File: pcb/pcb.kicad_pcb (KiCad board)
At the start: 2 copper layers, 8 parts, among them J1 Conn_01x04_Pin, J2 Conn_01x06_Pin, U1 XIAO-ESP32-C5-DIP, U17 AP2112K-3.3

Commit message: tidy up warnings
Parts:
- added R10: 10k, Resistor_THT:R_Axial_DIN0204_L3.6mm_D1.6mm_P5.08mm_Horizontal, F.Cu at (154.4, 117.5)
- added R11: 10k, Resistor_THT:R_Axial_DIN0204_L3.6mm_D1.6mm_P5.08mm_Horizontal, F.Cu at (154.4, 120.6)
- added R12: 10k, Resistor_THT:R_Axial_DIN0204_L3.6mm_D1.6mm_P5.08mm_Horizontal, F.Cu at (154.4, 123.8)
- added R13: 10k, Resistor_THT:R_Axial_DIN0204_L3.6mm_D1.6mm_P5.08mm_Horizontal, F.Cu at (162.4, 108.0)
- added R14: 10k, Resistor_THT:R_Axial_DIN0204_L3.6mm_D1.6mm_P5.08mm_Horizontal, F.Cu at (162.4, 111.2)
- added R15: 10k, Resistor_THT:R_Axial_DIN0204_L3.6mm_D1.6mm_P5.08mm_Horizontal, F.Cu at (162.4, 114.3)
- added R16: 10k, Resistor_THT:R_Axial_DIN0204_L3.6mm_D1.6mm_P5.08mm_Horizontal, F.Cu at (162.4, 117.5)
- added R17: 10k, Resistor_THT:R_Axial_DIN0204_L3.6mm_D1.6mm_P5.08mm_Horizontal, F.Cu at (162.4, 120.6)
- added R3: 10k, Resistor_THT:R_Axial_DIN0204_L3.6mm_D1.6mm_P5.08mm_Horizontal, F.Cu at (146.3, 114.3)
- added R4: 10k, Resistor_THT:R_Axial_DIN0204_L3.6mm_D1.6mm_P5.08mm_Horizontal, F.Cu at (146.3, 117.5)
- added R5: 10k, Resistor_THT:R_Axial_DIN0204_L3.6mm_D1.6mm_P5.08mm_Horizontal, F.Cu at (146.3, 120.6)
- added R6: 10k, Resistor_THT:R_Axial_DIN0204_L3.6mm_D1.6mm_P5.08mm_Horizontal, F.Cu at (146.3, 123.8)
- added R7: 10k, Resistor_THT:R_Axial_DIN0204_L3.6mm_D1.6mm_P5.08mm_Horizontal, F.Cu at (154.4, 108.0)
- added R8: 10k, Resistor_THT:R_Axial_DIN0204_L3.6mm_D1.6mm_P5.08mm_Horizontal, F.Cu at (154.4, 111.2)
- added R9: 10k, Resistor_THT:R_Axial_DIN0204_L3.6mm_D1.6mm_P5.08mm_Horizontal, F.Cu at (154.4, 114.3)
- added U10: XIAO-ESP32-C5-DIP, xiao_footprints:XIAO-ESP32-C5-DIP, F.Cu at (108.7, 66.0)
- added U11: XIAO-ESP32-C5-DIP, xiao_footprints:XIAO-ESP32-C5-DIP, F.Cu at (108.7, 86.4)
- added U12: XIAO-ESP32-C5-DIP, xiao_footprints:XIAO-ESP32-C5-DIP, F.Cu at (108.7, 106.7)
- added U13: XIAO-ESP32-C5-DIP, xiao_footprints:XIAO-ESP32-C5-DIP, F.Cu at (132.3, 45.7)
- added U14: XIAO-ESP32-C5-DIP, xiao_footprints:XIAO-ESP32-C5-DIP, F.Cu at (132.3, 66.0)
- added U15: XIAO-ESP32-C5-DIP, xiao_footprints:XIAO-ESP32-C5-DIP, F.Cu at (132.3, 86.4)
- added U18: XIAO-ESP32-C5-DIP, xiao_footprints:XIAO-ESP32-C5-DIP, F.Cu at (132.3, 106.7)
- added U2: XIAO-ESP32-C5-DIP, xiao_footprints:XIAO-ESP32-C5-DIP, F.Cu at (61.5, 66.0)
- added U3: XIAO-ESP32-C5-DIP, xiao_footprints:XIAO-ESP32-C5-DIP, F.Cu at (61.5, 86.4)
- added U4: XIAO-ESP32-C5-DIP, xiao_footprints:XIAO-ESP32-C5-DIP, F.Cu at (61.5, 106.7)
- added U5: XIAO-ESP32-C5-DIP, xiao_footprints:XIAO-ESP32-C5-DIP, F.Cu at (85.1, 45.7)
- added U6: XIAO-ESP32-C5-DIP, xiao_footprints:XIAO-ESP32-C5-DIP, F.Cu at (85.1, 66.0)
- added U7: XIAO-ESP32-C5-DIP, xiao_footprints:XIAO-ESP32-C5-DIP, F.Cu at (85.1, 86.4)
- added U8: XIAO-ESP32-C5-DIP, xiao_footprints:XIAO-ESP32-C5-DIP, F.Cu at (85.1, 106.7)
- added U9: XIAO-ESP32-C5-DIP, xiao_footprints:XIAO-ESP32-C5-DIP, F.Cu at (108.7, 45.7)
- moved BT1 69.0 mm to (57.4, 119.2)
- moved R1 67.4 mm to (146.3, 108.0)
- moved U1 60.9 mm to (61.5, 45.7), turned to 0 degrees
- moved J1 60.5 mm to (70.7, 119.2)
- moved R2 52.1 mm to (146.3, 111.2)
- moved U16 36.1 mm to (176.1, 44.3)
- moved J2 33.7 mm to (52.8, 119.2)
- moved U17 6.29 mm to (71.0, 131.5)
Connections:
- R2 pad 1: Net-(U1-GPIO25_D2) -> Net-(U1-3V3)
- R2 pad 2: Net-(U1-3V3) -> Net-(U1-GPIO25_D2)
- U16 pad 10: /GPS_RX -> /GPS_TX
- U16 pad 11: /GPS_TX -> Net-(U16-GPIO18)
- U16 pad 12: unconnected-(U16-GPIO8-Pad12) -> Net-(U16-GPIO8)
- U16 pad 15: unconnected-(U16-GPIO9-Pad15) -> Net-(U16-GPIO9)
- U16 pad 16: unconnected-(U16-GPIO10-Pad16) -> Net-(U15-GPIO25_D2)
- U16 pad 20: unconnected-(U16-GPIO14-Pad20) -> Net-(U16-GPIO14)
- U16 pad 22: GND -> unconnected-(U16-GND-Pad22)
- U16 pad 26: unconnected-(U16-GPIO1-Pad26) -> Net-(J2-Pin_1)
- U16 pad 27: unconnected-(U16-GPIO2-Pad27) -> Net-(U16-GPIO2)
- U16 pad 28: unconnected-(U16-GPIO42-Pad28) -> Net-(U10-GPIO25_D2)
- U16 pad 29: unconnected-(U16-GPIO41-Pad29) -> Net-(U11-GPIO25_D2)
- U16 pad 30: unconnected-(U16-GPIO40-Pad30) -> Net-(U12-GPIO25_D2)
- U16 pad 31: unconnected-(U16-GPIO39-Pad31) -> Net-(U13-GPIO25_D2)
- U16 pad 4: unconnected-(U16-GPIO4-Pad4) -> Net-(U1-GPIO25_D2)
- U16 pad 40: Net-(J2-Pin_1) -> Net-(U14-GPIO25_D2)
- U16 pad 44: unconnected-(U16-GND-Pad44) -> GND
- U16 pad 5: Net-(U1-GPIO25_D2) -> Net-(U16-GPIO5)
- U16 pad 6: unconnected-(U16-GPIO6-Pad6) -> Net-(U16-GPIO6)
- U16 pad 7: unconnected-(U16-GPIO7-Pad7) -> Net-(U16-GPIO7)
- U16 pad 8: unconnected-(U16-GPIO15-Pad8) -> Net-(U16-GPIO15)
- U16 pad 9: unconnected-(U16-GPIO16-Pad9) -> /GPS_RX

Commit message: more progress with the PCB layout
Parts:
- BT1: footprint Connector_PinHeader_2.54mm:PinHeader_1x02_P2.54mm_Horizontal -> Connector_PinHeader_2.54mm:PinHeader_1x02_P2.54mm_Vertical
- J1: footprint Connector_PinHeader_2.54mm:PinHeader_1x04_P2.54mm_Horizontal -> Connector_PinHeader_2.54mm:PinHeader_1x04_P2.54mm_Vertical
- moved R9 154.2 mm to (45.5, 223.5), turned to -90 degrees
- moved U16 149.2 mm to (90.0, 166.2)
- moved R8 135.4 mm to (46.9, 193.5), turned to -90 degrees
- moved R2 131.5 mm to (47.5, 24.5), turned to -90 degrees
- moved U8 128.6 mm to (31.4, 223.5), turned to 180 degrees
- moved BT1 123.1 mm to (137.0, 25.2)
- moved U7 122.9 mm to (32.4, 197.4), turned to 180 degrees
- moved U18 120.8 mm to (177.0, 218.9)
- moved R7 118.9 mm to (50.0, 165.0), turned to -90 degrees
- moved U15 117.9 mm to (177.0, 195.4)
- moved R3 117.6 mm to (47.5, 50.5), turned to -90 degrees
- moved U14 114.9 mm to (176.6, 172.0)
- moved U6 113.5 mm to (33.9, 167.4), turned to 180 degrees
- moved U13 109.1 mm to (175.6, 145.8)
- moved U5 107.1 mm to (32.4, 138.9), turned to 180 degrees
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
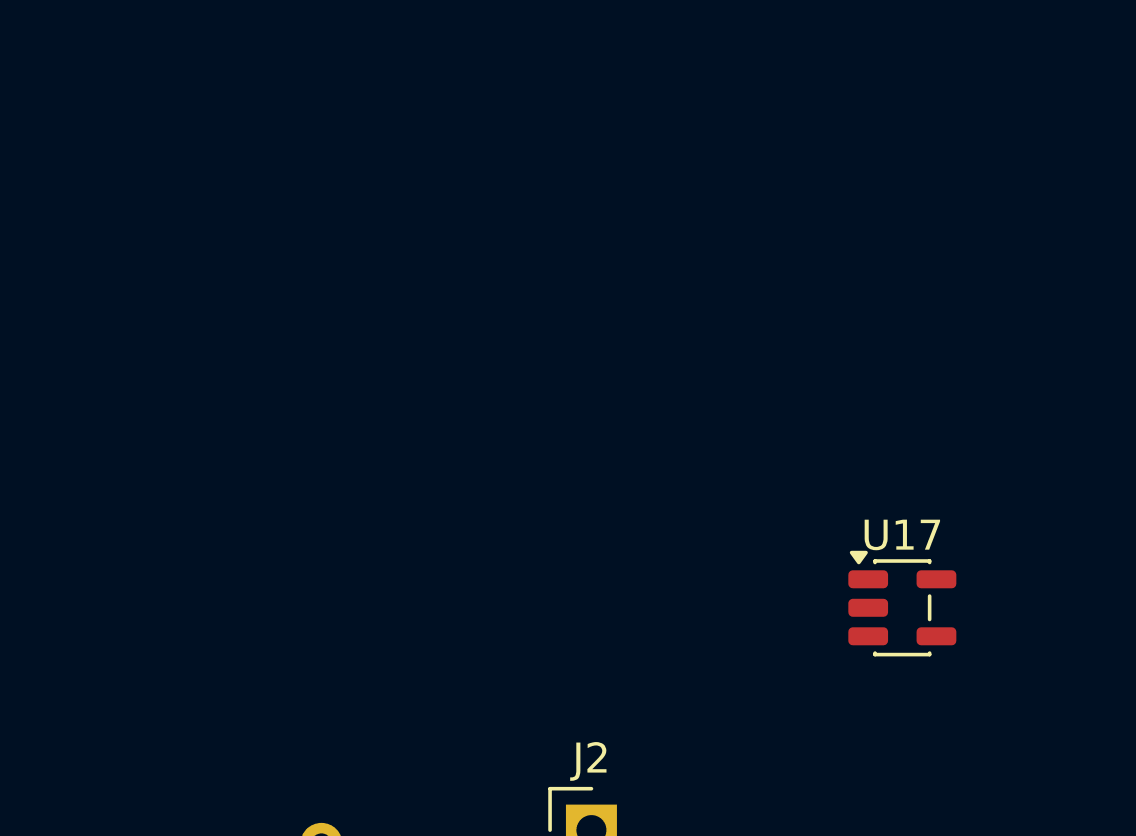
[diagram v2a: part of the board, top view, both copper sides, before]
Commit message: swap voltage regulator for an LD1117v33 regulator
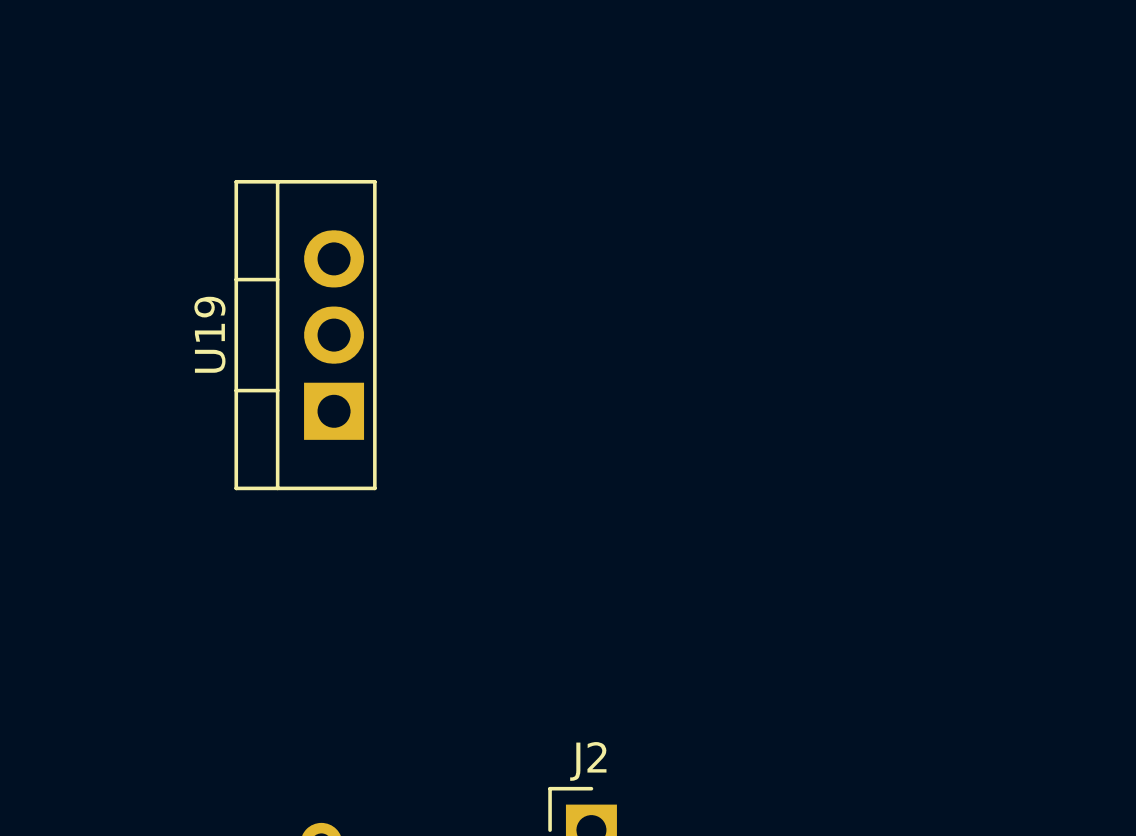
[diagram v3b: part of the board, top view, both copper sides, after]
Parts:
- removed U17: AP2112K-3.3, Package_TO_SOT_SMD:SOT-23-5
- added U19: LD1117V33, Package_TO_SOT_THT:TO-220-3_Vertical, F.Cu at (76.9, 44.0)

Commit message: more tweaks before routing
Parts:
- moved BT1 75.4 mm to (62.0, 17.5), turned to 90 degrees
- moved U9 54.3 mm to (123.4, 26.6)
- moved U18 53.9 mm to (123.4, 223.5)
- moved U10 53.8 mm to (123.4, 54.8)
- moved U15 53.7 mm to (123.4, 195.4)
- moved U11 53.6 mm to (123.4, 82.9)
- moved U14 53.4 mm to (123.4, 167.3)
- moved U12 53.3 mm to (123.4, 111.0)
- moved U13 52.6 mm to (123.4, 139.1)
- moved R12 52.4 mm to (108.2, 85.8)
- moved R13 51.7 mm to (108.2, 114.0)
- moved R15 49.8 mm to (108.2, 170.2)
- moved R14 49.6 mm to (108.2, 142.1)
- moved R17 48.8 mm to (108.2, 226.5)
- moved R11 48.3 mm to (108.2, 57.7)
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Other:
- board outline added: 130.9 x 223.4 mm
